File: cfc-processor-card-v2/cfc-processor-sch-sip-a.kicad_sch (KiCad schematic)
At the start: 20 parts, among them Q6 MMBT2907, U7 OSD3358-1G-ISM, U8 SN74AUC1G07DCKR, U9 TLVH431

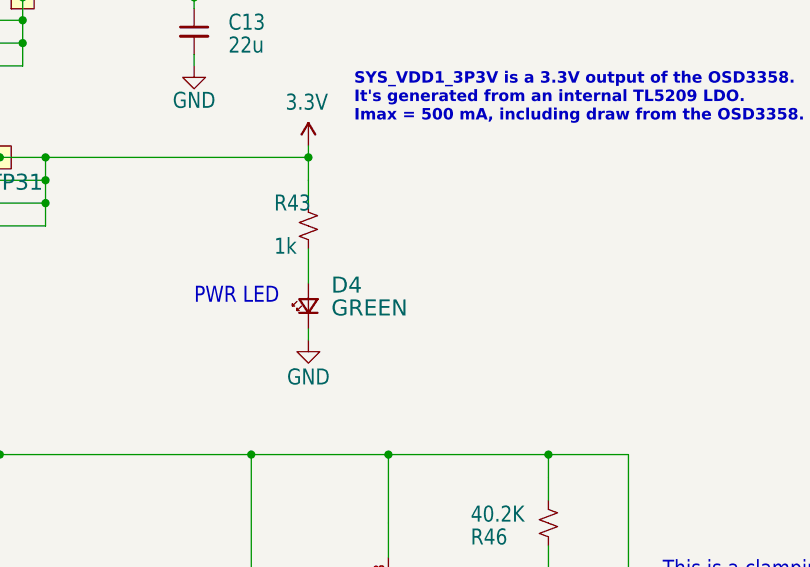
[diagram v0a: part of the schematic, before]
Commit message: Update
updated opd address resistors to 100 ohms from 100 ohms, changed the 100 ohm res VBUSP to 10 ohms. Updated TEC page for sensor to have bidirectional current sense for diag. Removed misc testpoints
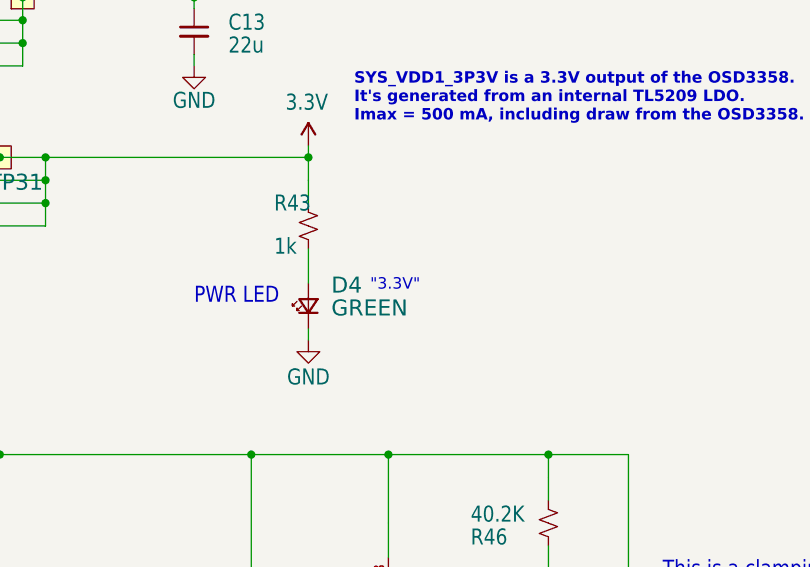
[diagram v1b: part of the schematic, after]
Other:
- note added: ""3.3V""
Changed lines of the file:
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@@
+		)
+	)
+	(text "\"3.3V\""
+		(exclude_from_sim no)
+		(at 229.108 88.646 0)
+		(effects
+			(font
+				(size 1.27 1.27)
+			)
+			(justify left bottom)
 		)
 	)

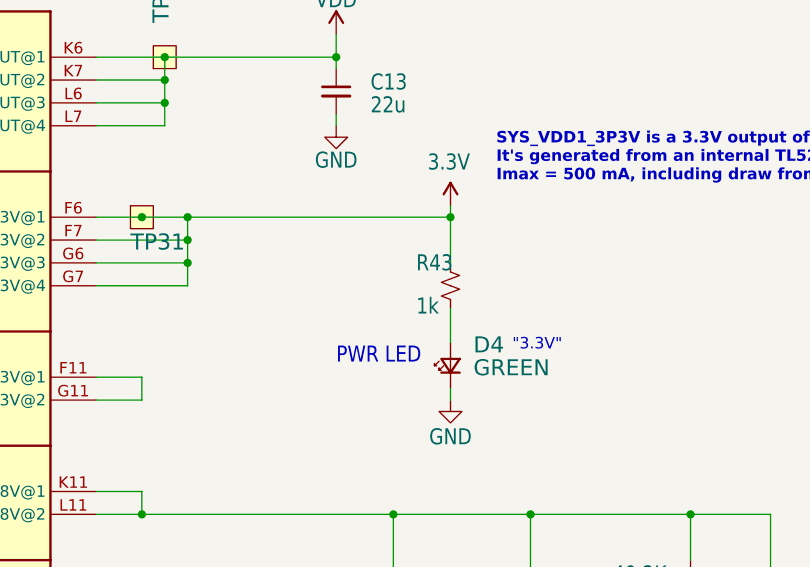
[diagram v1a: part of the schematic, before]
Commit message: Update
Updated OPD to align with proto card. Made changes from DR with Greenberg. Moved around polygon pours, led indicators, silkscreen issue date, etc. Ready for fab.
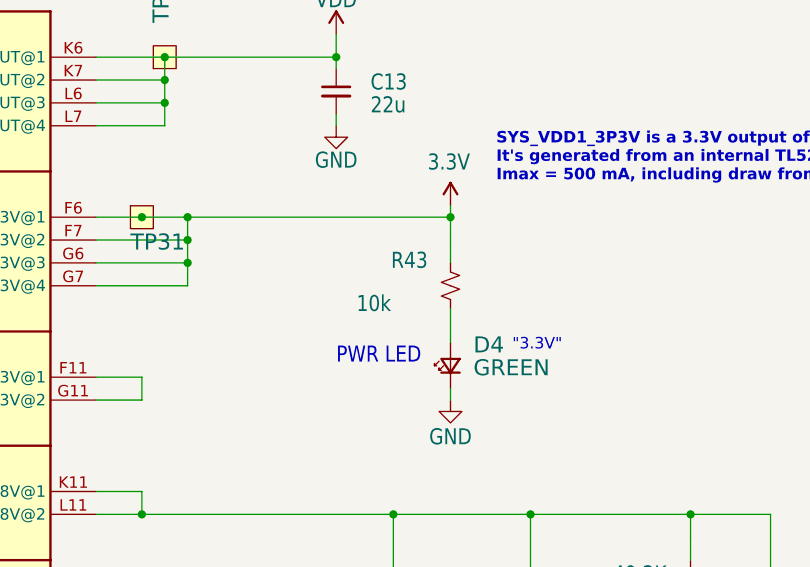
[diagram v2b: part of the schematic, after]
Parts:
- R43: value 1k -> 10k; DPN RMCF0603FT1K00CT-ND -> RMCF0603FT10K0CT-ND; MPN RMCF0603FT1K00 -> RMCF0603FT10K0
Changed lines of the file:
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@@
 	(title_block
 		(title "OreSat CFC Processor Card")
-		(date "2025-09-14")
-		(rev "2.0")
+		(date "2026-07-03")
+		(rev "2.1")
 		(company "Portland State Aerospace Society")
 	)
@@
 		(dnp no)
 		(property "Reference" "R43"
-			(at 218.44 79.7814 0)
+			(at 215.646 79.502 0)
 			(show_name no)
 			(do_not_autoplace no)
@@
 			)
 		)
-		(property "Value" "1k"
-			(at 218.44 84.582 0)
+		(property "Value" "10k"
+			(at 215.646 84.3026 0)
 			(show_name no)
 			(do_not_autoplace no)
@@
 					(size 1.778 1.5113)
 				)
-				(justify left bottom)
+				(justify right bottom)
 			)
 		)
@@
 			)
 		)
-		(property "DPN" "RMCF0603FT1K00CT-ND"
+		(property "DPN" "RMCF0603FT10K0CT-ND"
 			(at 222.25 81.28 0)
 			(hide yes)
@@
 			)
 		)
-		(property "MPN" "RMCF0603FT1K00"
+		(property "MPN" "RMCF0603FT10K0"
 			(at 222.25 81.28 0)
 			(hide yes)

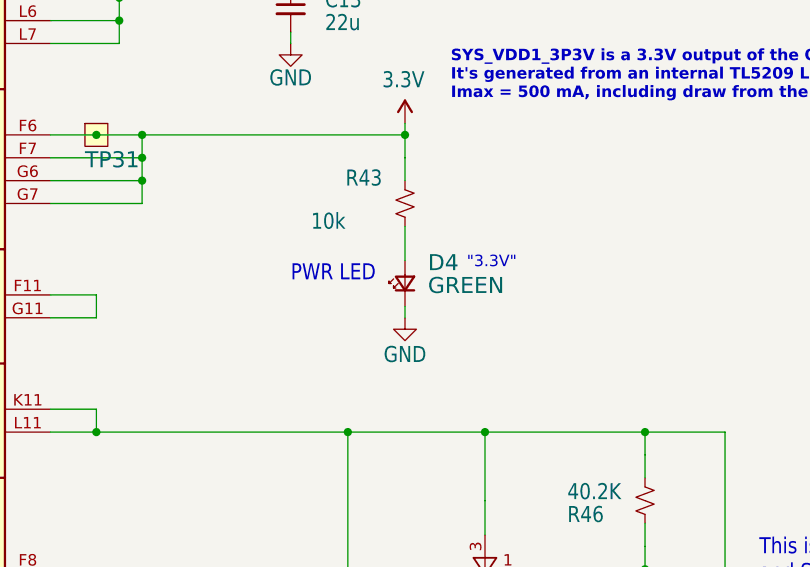
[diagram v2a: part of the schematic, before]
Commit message: Update
Updated BOM, couple of fixes on OPD. Minor routing and layout changes. Removed logic gates from sensor card.
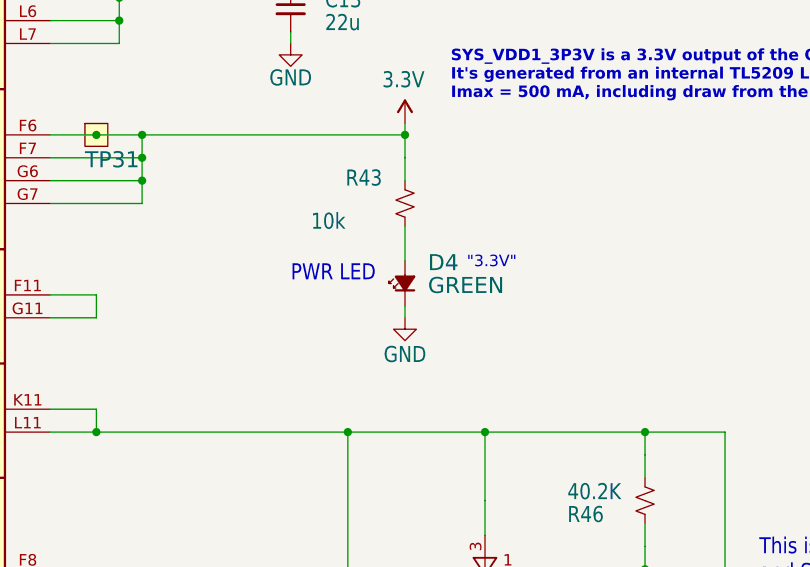
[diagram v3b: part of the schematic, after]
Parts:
- C11, C12, C13: DPN 490-GCM32EC71E226KE36KCT-ND -> 587-5949-1-ND; MFR Murata Electronics -> Taiyo Yuden; MPN GCM32EC71E226KE36K -> TMK325B7226KMHP
- C14, C15: DPN 587-3472-1-ND -> 399-6856-1-ND; MFR Taiyo Yuden -> KEMET; MPN TMK107BJ104KAHT -> C0603C104K5RACAUTO
- D4: symbol Device:LED_Small -> Device:LED_Small_Filled
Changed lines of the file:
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@@
 			)
 		)
-		(property "Description" "Unpolarized capacitor, small symbol"
+		(property "Description" "0.1 µF ±10% 50V Ceramic Capacitor X7R 0603 (1608 Metric)"
 			(at 234.95 222.25 0)
 			(hide yes)
@@
 			)
 		)
-		(property "DPN" "587-3472-1-ND"
+		(property "DPN" "399-6856-1-ND"
 			(at 234.95 222.25 0)
 			(hide yes)
@@
 			)
 		)
-		(property "MFR" "Taiyo Yuden"
+		(property "MFR" "KEMET"
 			(at 234.95 222.25 0)
 			(hide yes)
@@
 			)
 		)
-		(property "MPN" "TMK107BJ104KAHT"
+		(property "MPN" "C0603C104K5RACAUTO"
 			(at 234.95 222.25 0)
 			(hide yes)
@@
 	)
 	(symbol
-		(lib_id "Device:LED_Small")
+		(lib_id "Device:LED_Small_Filled")
 		(at 222.25 90.17 90)
 		(unit 1)
@@
 			)
 		)
-		(property "Description" "Light emitting diode, small symbol"
+		(property "Description" "Light emitting diode, small symbol, filled shape"
 			(at 222.25 90.17 0)
 			(hide yes)
@@
 			)
 		)
-		(property "Description" "Unpolarized capacitor, small symbol"
+		(property "Description" "0.1 µF ±10% 50V Ceramic Capacitor X7R 0603 (1608 Metric)"
 			(at 257.81 187.96 0)
 			(hide yes)
@@
 			)
 		)
-		(property "DPN" "587-3472-1-ND"
+		(property "DPN" "399-6856-1-ND"
 			(at 257.81 187.96 0)
 			(hide yes)
@@
 			)
 		)
-		(property "MFR" "Taiyo Yuden"
+		(property "MFR" "KEMET"
 			(at 257.81 187.96 0)
 			(hide yes)
@@
 			)
 		)
-		(property "MPN" "TMK107BJ104KAHT"
+		(property "MPN" "C0603C104K5RACAUTO"
 			(at 257.81 187.96 0)
 			(hide yes)
@@
 			)
 		)
-		(property "Description" "Unpolarized capacitor, small symbol"
+		(property "Description" "22 µF ±10% 25V Ceramic Capacitor X7R 1210 (3225 Metric)"
 			(at 209.55 59.69 0)
 			(hide yes)
@@
 			)
 		)
-		(property "DPN" "490-GCM32EC71E226KE36KCT-ND"
+		(property "DPN" "587-5949-1-ND"
 			(at 209.55 59.69 0)
 			(hide yes)
@@
 			)
 		)
-		(property "MFR" "Murata Electronics"
+		(property "MFR" "Taiyo Yuden"
 			(at 209.55 59.69 0)
 			(hide yes)
@@
 			)
 		)
-		(property "MPN" "GCM32EC71E226KE36K"
+		(property "MPN" "TMK325B7226KMHP"
 			(at 209.55 59.69 0)
 			(hide yes)
@@
 			)
 		)
-		(property "Description" "Unpolarized capacitor, small symbol"
+		(property "Description" "22 µF ±10% 25V Ceramic Capacitor X7R 1210 (3225 Metric)"
 			(at 91.44 78.74 0)
 			(hide yes)
@@
 			)
 		)
-		(property "DPN" "490-GCM32EC71E226KE36KCT-ND"
+		(property "DPN" "587-5949-1-ND"
 			(at 91.44 78.74 0)
 			(hide yes)
@@
 			)
 		)
-		(property "MFR" "Murata Electronics"
+		(property "MFR" "Taiyo Yuden"
 			(at 91.44 78.74 0)
 			(hide yes)
@@
 			)
 		)
-		(property "MPN" "GCM32EC71E226KE36K"
+		(property "MPN" "TMK325B7226KMHP"
 			(at 91.44 78.74 0)
 			(hide yes)
@@
 			)
 		)
-		(property "Description" "Unpolarized capacitor, small symbol"
+		(property "Description" "22 µF ±10% 25V Ceramic Capacitor X7R 1210 (3225 Metric)"
 			(at 86.36 60.96 0)
 			(hide yes)
@@
 			)
 		)
-		(property "DPN" "490-GCM32EC71E226KE36KCT-ND"
+		(property "DPN" "587-5949-1-ND"
 			(at 86.36 60.96 0)
 			(hide yes)
@@
 			)
 		)
-		(property "MFR" "Murata Electronics"
+		(property "MFR" "Taiyo Yuden"
 			(at 86.36 60.96 0)
 			(hide yes)
@@
 			)
 		)
-		(property "MPN" "GCM32EC71E226KE36K"
+		(property "MPN" "TMK325B7226KMHP"
 			(at 86.36 60.96 0)
 			(hide yes)

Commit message: Small update
Fixed minor issue with voltage clamp on usb line. Added nreset clamp and changed VBUS pin to USB voltage bus
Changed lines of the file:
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@@
+	)
+	(junction
+		(at 259.08 218.44)
+		(diameter 0)
+		(color 0 0 0 0)
 	)
 	(junction
@@
 	(wire
 		(pts
+			(xy 259.08 218.44) (xy 259.08 229.87)
+		)
+		(stroke
+			(width 0)
+			(type default)
+		)
+	)
+	(wire
+		(pts
 			(xy 193.04 78.74) (xy 193.04 81.28)
 		)
@@
 	(wire
 		(pts
-			(xy 234.95 218.44) (xy 245.11 218.44)
+			(xy 234.95 218.44) (xy 259.08 218.44)
 		)
 		(stroke
@@
 		(pts
 			(xy 222.25 73.66) (xy 193.04 73.66)
+		)
+		(stroke
+			(width 0.1524)
+			(type solid)
+		)
+	)
+	(wire
+		(pts
+			(xy 259.08 218.44) (xy 262.89 218.44)
 		)
 		(stroke
@@
 			)
 			(justify left bottom)
+		)
+	)
+	(hierarchical_label "nRESET_CLAMP"
+		(shape output)
+		(at 259.08 229.87 270)
+		(effects
+			(font
+				(size 1.27 1.27)
+			)
+			(justify right)
 		)
 	)
@@
 	(hierarchical_label "NRESET"
 		(shape input)
-		(at 245.11 218.44 0)
+		(at 262.89 218.44 0)
 		(effects
 			(font
